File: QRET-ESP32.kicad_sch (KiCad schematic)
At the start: 32 parts, among them J1 Conn_01x04_Socket, J10 Conn_01x02, J11 Conn_01x02, J4 Conn_02x04_Counter_Clockwise, J5 Conn_01x02_Socket, J6 Conn_01x02_Socket, J7 Conn_01x02_Socket, J8 Conn_01x02_Socket, J9 Conn_01x02_Socket, Q1 PNP, Q2 PNP, U1 ESP32-S2-DevKitC-1, U2 ADS1115IDGS

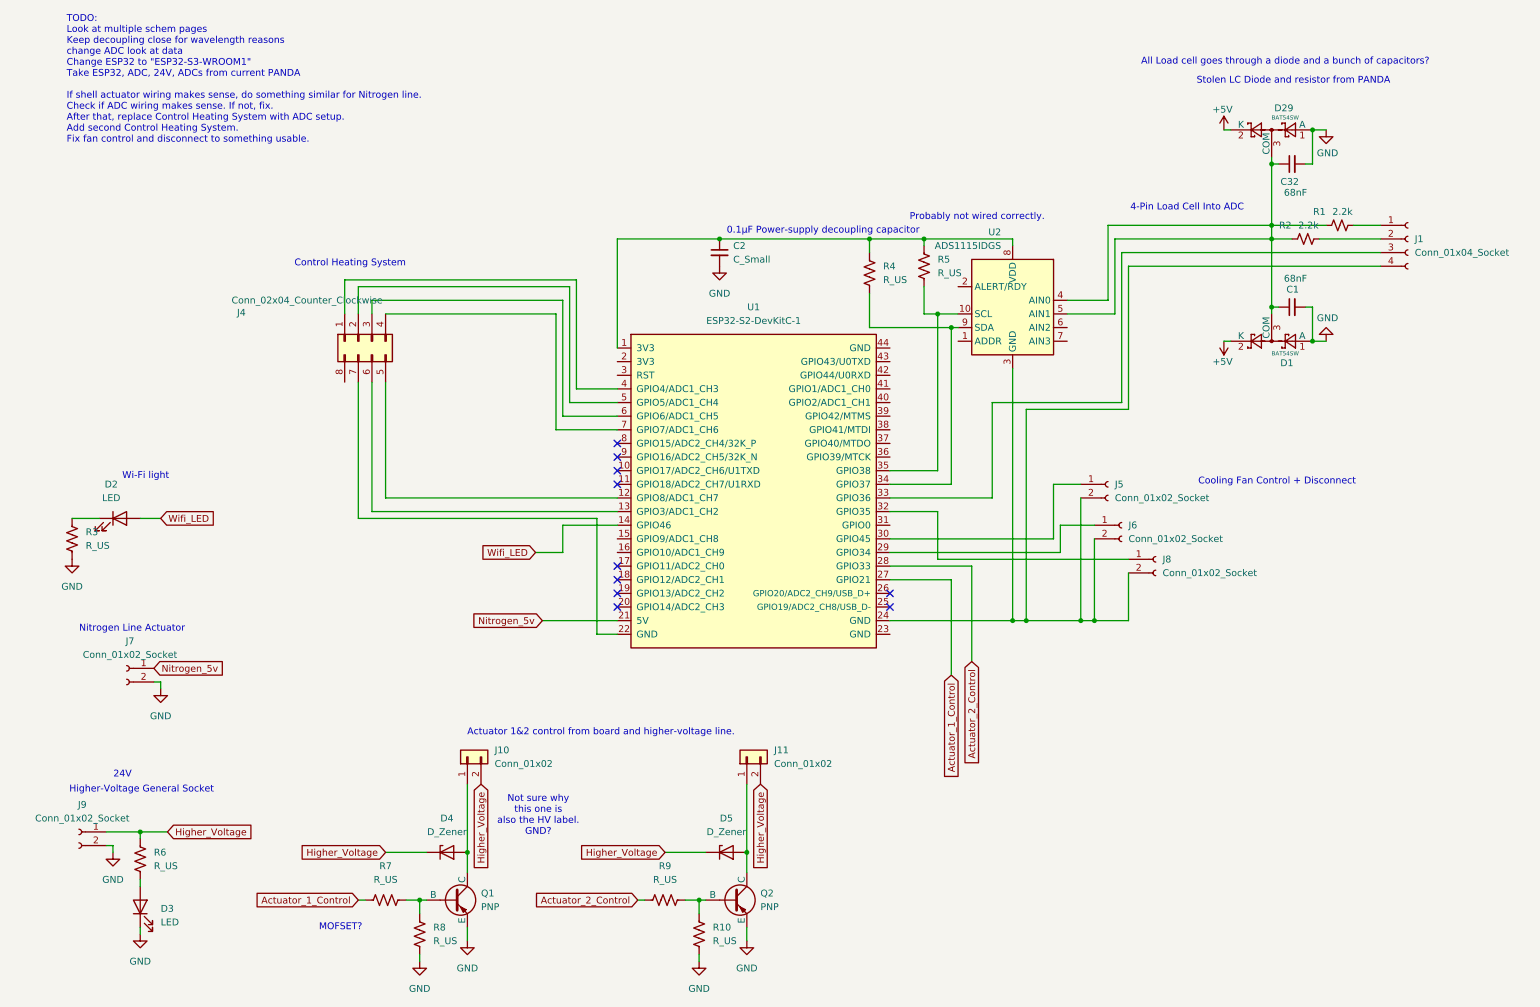
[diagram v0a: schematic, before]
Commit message: Stole a bunch more stuff from PANDA, added fan and heating line
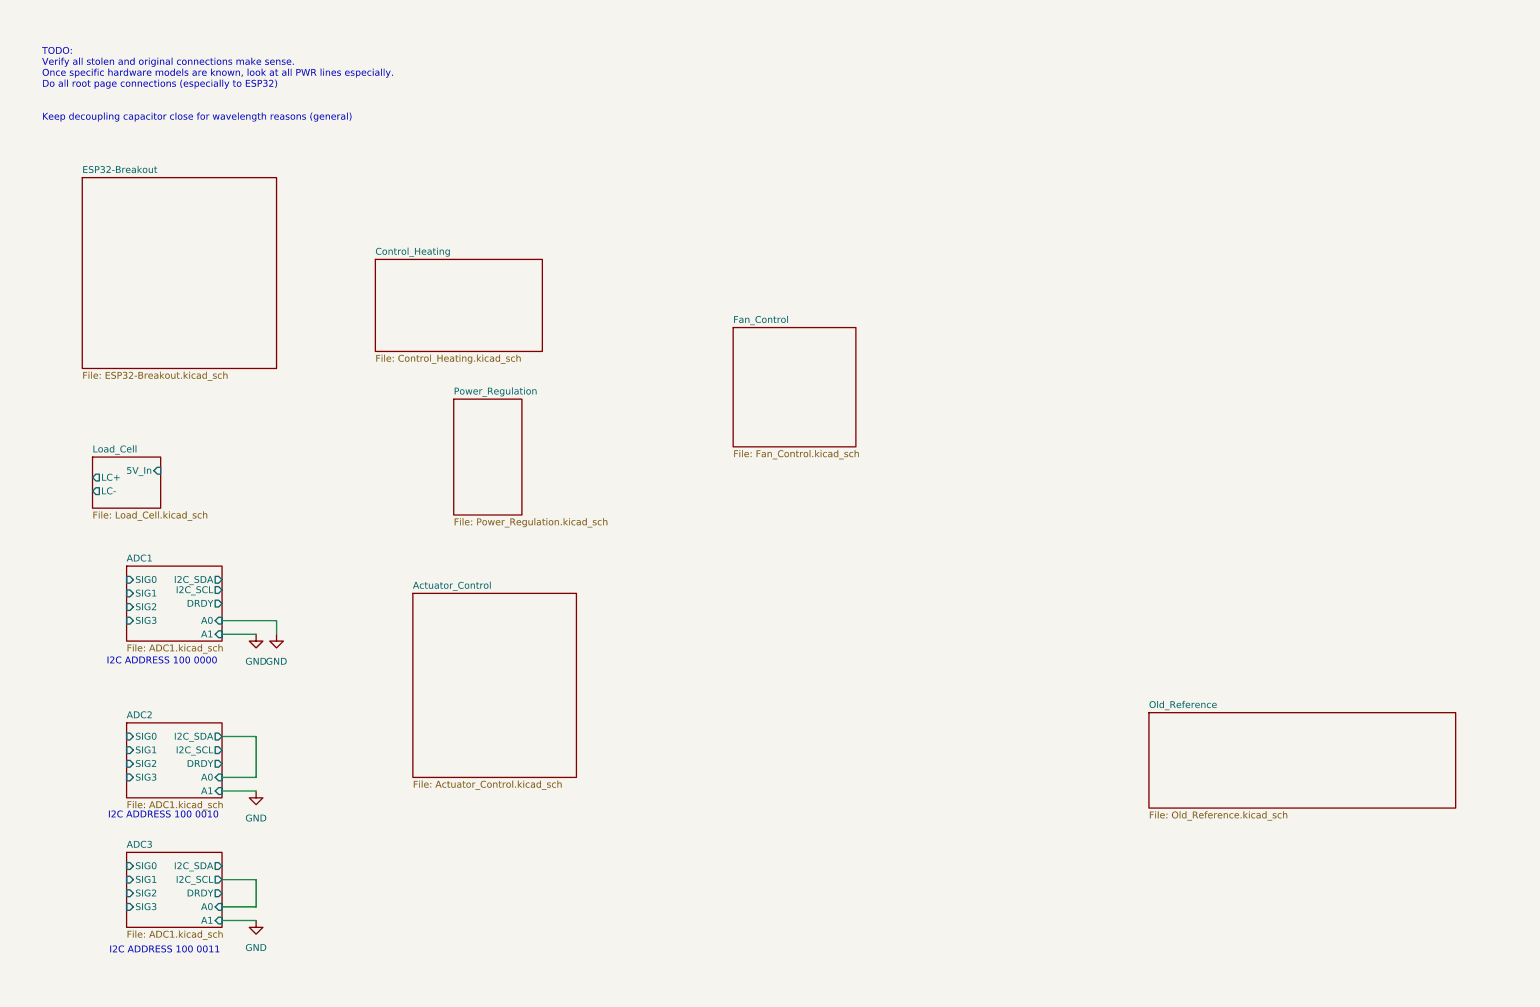
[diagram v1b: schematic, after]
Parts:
- removed C1, C32: 68nF, Capacitor_SMD:C_0805_2012Metric, symbol Device:C_Small
- removed C2: C_Small, symbol Device:C_Small
- removed D1, D29: BAT54SW, Package_TO_SOT_SMD:SOT-323_SC-70, symbol Diode:BAT54SW
- removed D2, D3: LED, symbol Device:LED
- removed D4, D5: D_Zener, symbol Device:D_Zener
- removed J1: Conn_01x04_Socket, Connector_JST:JST_EH_B4B-EH-A_1x04_P2.50mm_Vertical, symbol Connector:Conn_01x04_Socket
- removed J10, J11: Conn_01x02, symbol Connector_Generic:Conn_01x02
- removed J4: Conn_02x04_Counter_Clockwise, Connector_JST:JST_J2100_B08B-J21DK-GGXR_2x04_P2.50x4.00mm_Vertical, symbol Connector_Generic:Conn_02x04_Counter_Clockwise
- removed J5, J6, J7: Conn_01x02_Socket, Connector_JST:JST_EH_B2B-EH-A_1x02_P2.50mm_Vertical, symbol Connector:Conn_01x02_Socket
- removed J8, J9: Conn_01x02_Socket, symbol Connector:Conn_01x02_Socket
- removed Q1, Q2: PNP, symbol Simulation_SPICE:PNP
- removed R1, R2: 2.2k, Resistor_SMD:R_0402_1005Metric, symbol Device:R_Small_US
- removed R10, R3, R4, R5, R6, R7, R8, R9: R_US, symbol Device:R_US
- removed U1: ESP32-S2-DevKitC-1, PCM_Espressif:ESP32-S2-DevKitC-1, symbol PCM_Espressif:ESP32-S2-DevKitC-1
- removed U2: ADS1115IDGS, Package_SO:TSSOP-10_3x3mm_P0.5mm, symbol Analog_ADC:ADS1115IDGS
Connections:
- no-connect marks 10 -> 0
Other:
- added sheet ADC1 (ADC1.kicad_sch)
- added sheet ADC2 (ADC1.kicad_sch)
- added sheet ADC3 (ADC1.kicad_sch)
- added sheet Actuator_Control (Actuator_Control.kicad_sch)
- added sheet Control_Heating (Control_Heating.kicad_sch)
- added sheet ESP32-Breakout (ESP32-Breakout.kicad_sch)
- added sheet Fan_Control (Fan_Control.kicad_sch)
- added sheet Load_Cell (Load_Cell.kicad_sch)
- added sheet Old_Reference (Old_Reference.kicad_sch)
- added sheet Power_Regulation (Power_Regulation.kicad_sch)
- note added: "I2C ADDRESS 100 0000"
- note added: "I2C ADDRESS 100 0010"
- note added: "I2C ADDRESS 100 0011"
- note added: "TODO: Verify all stolen and original connections make sense. Once specific hardware models are known, look at all PWR lines especially. Do all root page connections (especially to ESP32) Keep decoupling capacitor close for wavelength reasons (general)"
- note removed: "0.1μF Power-supply decoupling capacitor"
- note removed: "24V"
- note removed: "4-Pin Load Cell Into ADC"
- note removed: "Actuator 1&2 control from board and higher-voltage line."
- note removed: "All Load cell goes through a diode and a bunch of capacitors?"
- note removed: "Control Heating System"
- note removed: "Cooling Fan Control + Disconnect"
- note removed: "Higher-Voltage General Socket"
- note removed: "MOFSET?"
- note removed: "Nitrogen Line Actuator"
- note removed: "Not sure why this one is also the HV label. GND?"
- note removed: "Probably not wired correctly."
- note removed: "Stolen LC Diode and resistor from PANDA"
- note removed: "TODO: Look at multiple schem pages Keep decoupling close for wavelength reasons change ADC look at data Change ESP32 to "ESP32-S3-WROOM1" Take ESP32, ADC, 24V, ADCs from current PANDA If shell actuator wiring makes sense, do something similar for Nitrogen line. Check if ADC wiring makes sense. If not, fix. After that, replace Control Heating System with ADC setup. Add second Control Heating Syste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"
- note removed: "Wi-Fi light"

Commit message: Updated most of root-page labels.
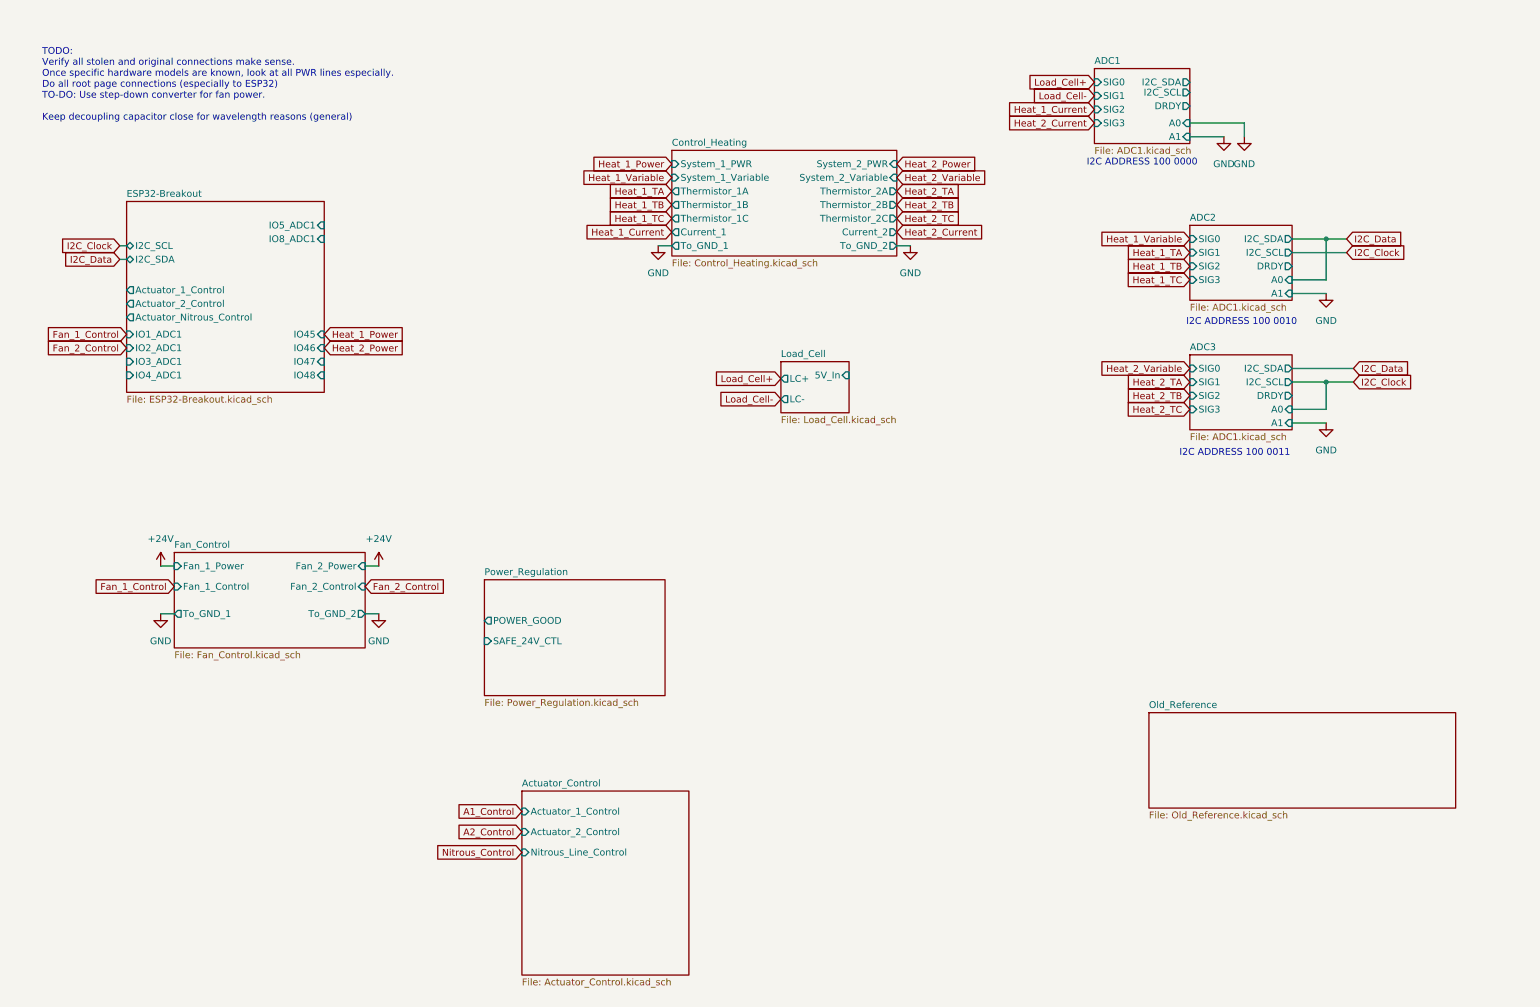
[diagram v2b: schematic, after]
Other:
- sheet Actuator_Control ports: added Actuator_1_Control, Actuator_2_Control, Nitrous_Line_Control; removed none
- sheet Control_Heating ports: added Current_1, Current_2, System_1_PWR, System_1_Variable, System_2_PWR, System_2_Variable, Thermistor_1A, Thermistor_1B, Thermistor_1C, Thermistor_2A, Thermistor_2B, Thermistor_2C, To_GND_1, To_GND_2; removed none
- sheet ESP32-Breakout ports: added Actuator_1_Control, Actuator_2_Control, Actuator_Nitrous_Control, I2C_SCL, I2C_SDA, IO1_ADC1, IO2_ADC1, IO3_ADC1, IO45, IO46, IO47, IO48, IO4_ADC1, IO5_ADC1, IO8_ADC1; removed none
- sheet Fan_Control ports: added Fan_1_Control, Fan_1_Power, Fan_2_Control, Fan_2_Power, To_GND_1, To_GND_2; removed none
- sheet Power_Regulation ports: added POWER_GOOD, SAFE_24V_CTL; removed none
- note added: "TODO: Verify all stolen and original connections make sense. Once specific hardware models are known, look at all PWR lines especially. Do all root page connections (especially to ESP32) TO-DO: Use step-down converter for fan power. Keep decoupling capacitor close for wavelength reasons (general)"
- note removed: "TODO: Verify all stolen and original connections make sense. Once specific hardware models are known, look at all PWR lines especially. Do all root page connections (especially to ESP32) Keep decoupling capacitor close for wavelength reasons (general)"

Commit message: Added 24V-12V step-down converter for fans, started switch to devkit.
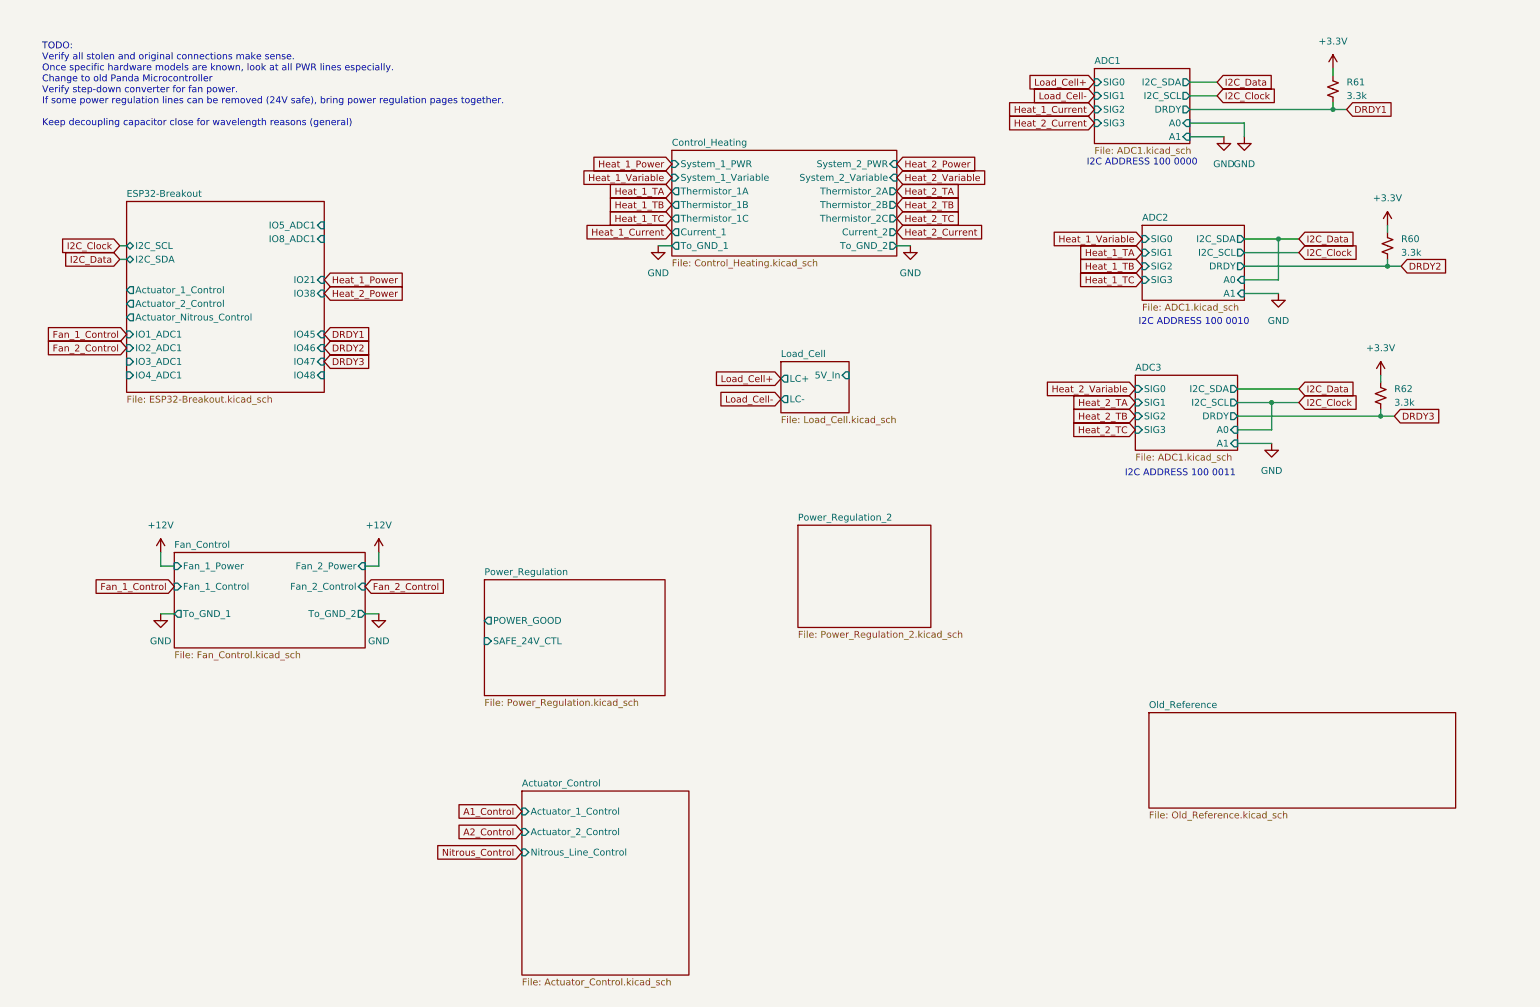
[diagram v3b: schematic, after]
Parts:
- added R60, R61, R62: 3.3k, symbol Device:R_Small_US
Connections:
- new net +3.3V: R60.1, R61.1, R62.1
- new net DRDY1: R61.2
- new net DRDY2: R60.2
- new net DRDY3: R62.2
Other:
- added sheet Power_Regulation_2 (Power_Regulation_2.kicad_sch)
- sheet ESP32-Breakout ports: added IO21, IO38; removed none
- note added: "TODO: Verify all stolen and original connections make sense. Once specific hardware models are known, look at all PWR lines especially. Change to old Panda Microcontroller Verify step-down converter for fan power. If some power regulation lines can be removed (24V safe), bring power regulation pages together. Keep decoupling capacitor close for wavelength reasons (general)"
- note removed: "TODO: Verify all stolen and original connections make sense. Once specific hardware models are known, look at all PWR lines especially. Do all root page connections (especially to ESP32) TO-DO: Use step-down converter for fan power. Keep decoupling capacitor close for wavelength reasons (general)"

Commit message: Updated to 4-pin fans, moved power pages together, deleted old reference.
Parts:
- R1: renamed from R61; footprint (none) -> Resistor_SMD:R_0402_1005Metric
- R2: renamed from R62; footprint (none) -> Resistor_SMD:R_0402_1005Metric
- R3: renamed from R60; footprint (none) -> Resistor_SMD:R_0402_1005Metric
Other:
- removed sheet Old_Reference
- removed sheet Power_Regulation_2
- sheet ESP32-Breakout ports: added DRDY1, DRDY2, DRDY3, Fan_1_Control, Fan_1_PWM, Fan_2_Control, Fan_2_PWM, Heat_1_Power, Heat_2_Power; removed IO1_ADC1, IO21, IO2_ADC1, IO38, IO3_ADC1, IO45, IO46, IO47, IO48, IO4_ADC1, IO5_ADC1, IO8_ADC1
- sheet Fan_Control ports: added Fan_1_PWM, Fan_2_PWM; removed none
- sheet Power_Regulation ports: added 12_POWER_GOOD, 24_POWER_GOOD; removed POWER_GOOD, SAFE_24V_CTL
- note added: "TODO: Verify all stolen and original connections make sense. Once specific hardware models are known, look at all PWR lines especially. Change to old Panda Microcontroller Verify step-down converter for fan power. If some power regulation lines can be removed (24V safe), bring power regulation pages together. Keep decoupling capacitor close for wavelength reasons (general) Nix All Safe_24 Remove 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"
- note removed: "TODO: Verify all stolen and original connections make sense. Once specific hardware models are known, look at all PWR lines especially. Change to old Panda Microcontroller Verify step-down converter for fan power. If some power regulation lines can be removed (24V safe), bring power regulation pages together. Keep decoupling capacitor close for wavelength reasons (general)"
